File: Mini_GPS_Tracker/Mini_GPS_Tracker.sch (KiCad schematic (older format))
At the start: 23 parts, among them J1 USB_C_Receptacle, J4 Conn_ARM_JTAG_SWD_10, SW1 SW_Push, U1 CH340E, Y1 Crystal

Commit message: updates to routing and fix commit
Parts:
- removed U1: CH340E, Sparkfun-Artemis:MSOP10, symbol Sparkfun~Artemis:CH340E
- added C20: 100 nf, Capacitor_SMD:C_0805_2012Metric, symbol Device:C
- added U1: FT230XS, Package_SO:SSOP-16_3.9x4.9mm_P0.635mm, symbol Interface_USB:FT230XS
- C6, C7: value CAP -> 15 pf
- J4: footprint Connector_PinHeader_1.00mm:PinHeader_2x05_P1.00mm_Vertical -> Connector_PinHeader_2.54mm:PinHeader_2x05_P2.54mm_Vertical
- LS1: symbol Sparkfun~Artemis:CSS-J4D20-SMT -> Mini_GPS_Tracker-rescue:CSS-J4D20-SMT-Sparkfun_Artemis-Mini_GPS_Tracker-rescue
- MD1: symbol Sparkfun~Artemis:SPARKFUN_WRL-15376 -> Mini_GPS_Tracker-rescue:SPARKFUN_WRL-15376-Sparkfun_Artemis-Mini_GPS_Tracker-rescue
- R7: value R -> 0 ohm
- Y1: value Crystal -> 32.786 KHz
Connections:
- wire segments 117 -> 128
- no-connect marks 46 -> 48
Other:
- moved on the sheet: D1, D2, R4, R5, R7

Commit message: Add files via upload
Updates schematics
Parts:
- removed C20: 100 nf, Capacitor_SMD:C_0805_2012Metric, symbol Device:C
- removed C3: 0.1uF, Capacitor_SMD:C_0805_2012Metric_Pad1.15x1.40mm_HandSolder, symbol pspice:CAP
- removed C5: 10nF, Capacitor_SMD:C_0805_2012Metric_Pad1.15x1.40mm_HandSolder, symbol pspice:CAP
- removed C6, C7: 15 pf, Capacitor_SMD:C_0805_2012Metric_Pad1.15x1.40mm_HandSolder, symbol pspice:CAP
- removed D1, D2: LED, LED_SMD:LED_0805_2012Metric_Pad1.15x1.40mm_HandSolder, symbol Device:LED
- removed MD1: SPARKFUN_WRL-15376, Sparkfun-Artemis:SPARKFUN_WRL-15376, symbol Mini_GPS_Tracker-rescue:SPARKFUN_WRL-15376-Sparkfun_Artemis-Mini_GPS_Tracker-re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
- removed R4, R5: 1K, Resistor_SMD:R_0805_2012Metric_Pad1.15x1.40mm_HandSolder, symbol Device:R
- removed U1: FT230XS, Package_SO:SSOP-16_3.9x4.9mm_P0.635mm, symbol Interface_USB:FT230XS
- removed Y1: 32.786 KHz, Crystal:Crystal_SMD_2012-2Pin_2.0x1.2mm_HandSoldering, symbol Device:Crystal
- added C22: 100nF, symbol pspice:CAP
- added J5: Qwiic_Connector, SPARKX_1X04_1MM_RA, symbol SparkFun_SchematicComponents:Qwiic_Connector
- added U12: FT230XS, Package_SO:SSOP-16_3.9x4.9mm_P0.635mm, symbol Interface_USB:FT230XS
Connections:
- net +3V3: now also J5.2 (VCC), U12.12 (VCC)
- net GND: now also C22.1, J5.1 (GND), U12.13 (GND), U12.5 (GND)
- net RTS: now also U12.2 (~RTS)
- net at J1.A7 (D-): now also U12.9 (USBDM)
- net at J1.B7 (D-): now also U12.8 (USBDP)
- new net: C22.2, U12.10 (3V3OUT), U12.11 (~RESET), U12.3 (VCCIO)
- new net QWIIC_SCL: J5.4 (SCL)
- new net QWIIC_SDA: J5.3 (SDA)
- new net USB_RXI: U12.4 (RXD)
- new net USB_TX0: U12.1 (TXD)
- no-connect marks 48 -> 15
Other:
- moved on the sheet: LS1, R7

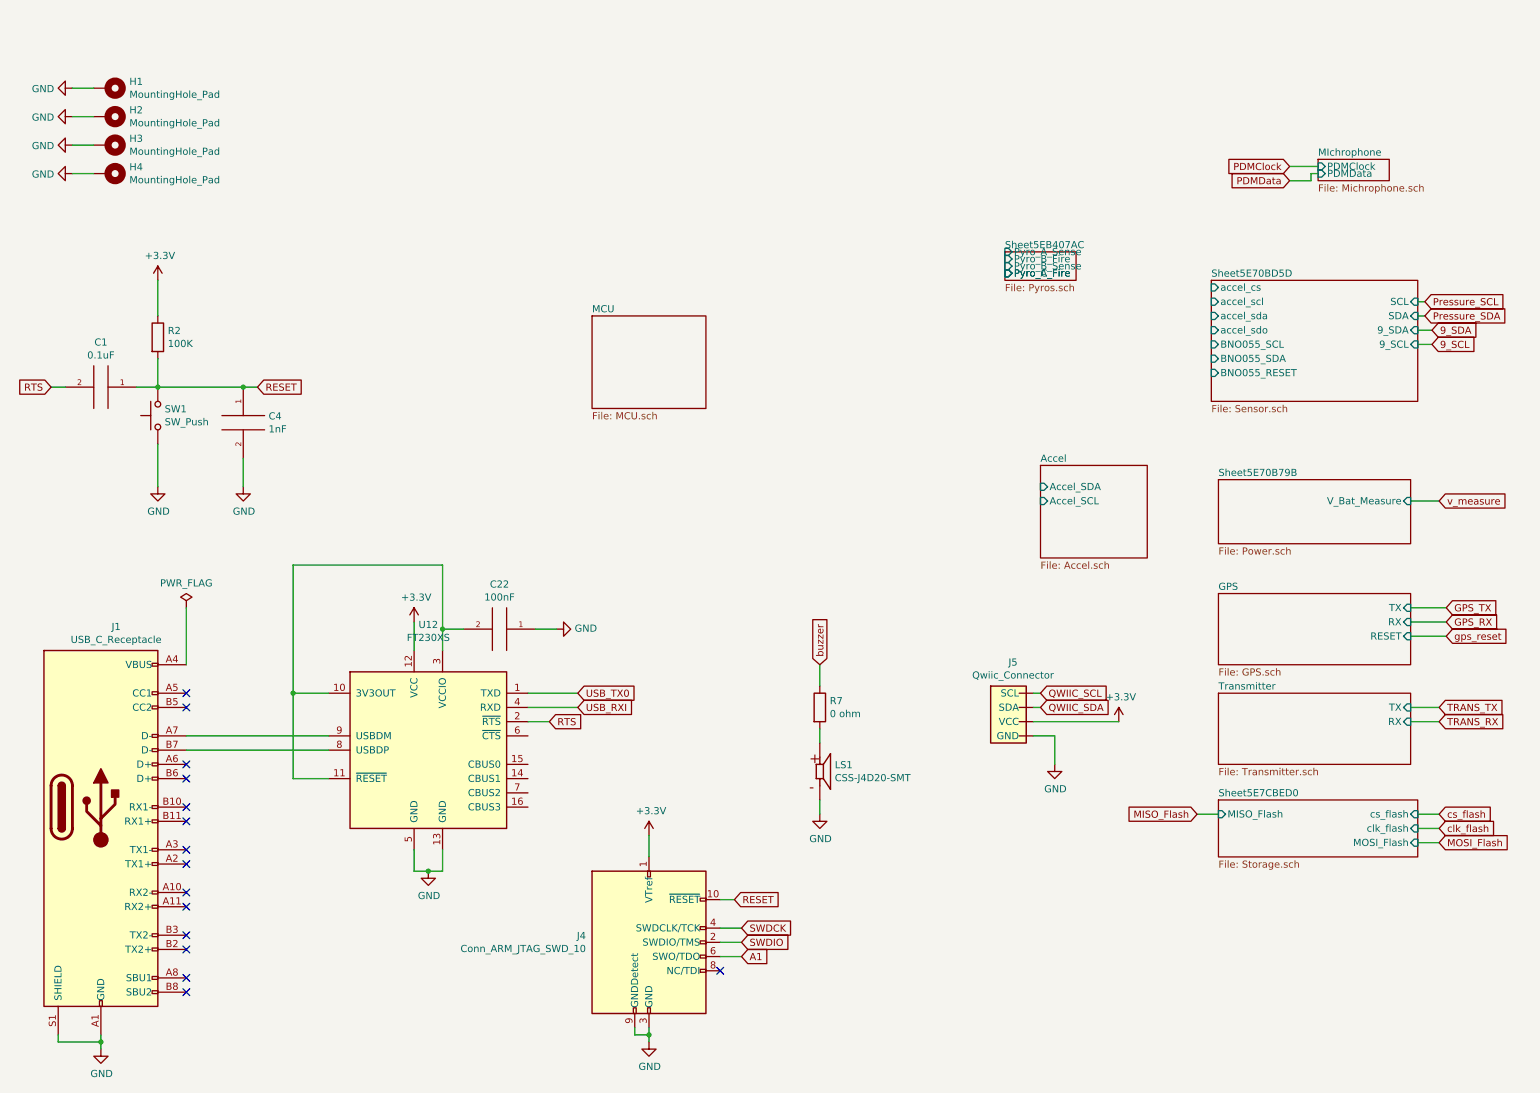
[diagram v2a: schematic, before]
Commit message: Add files via upload
Adding 100 pin MCU
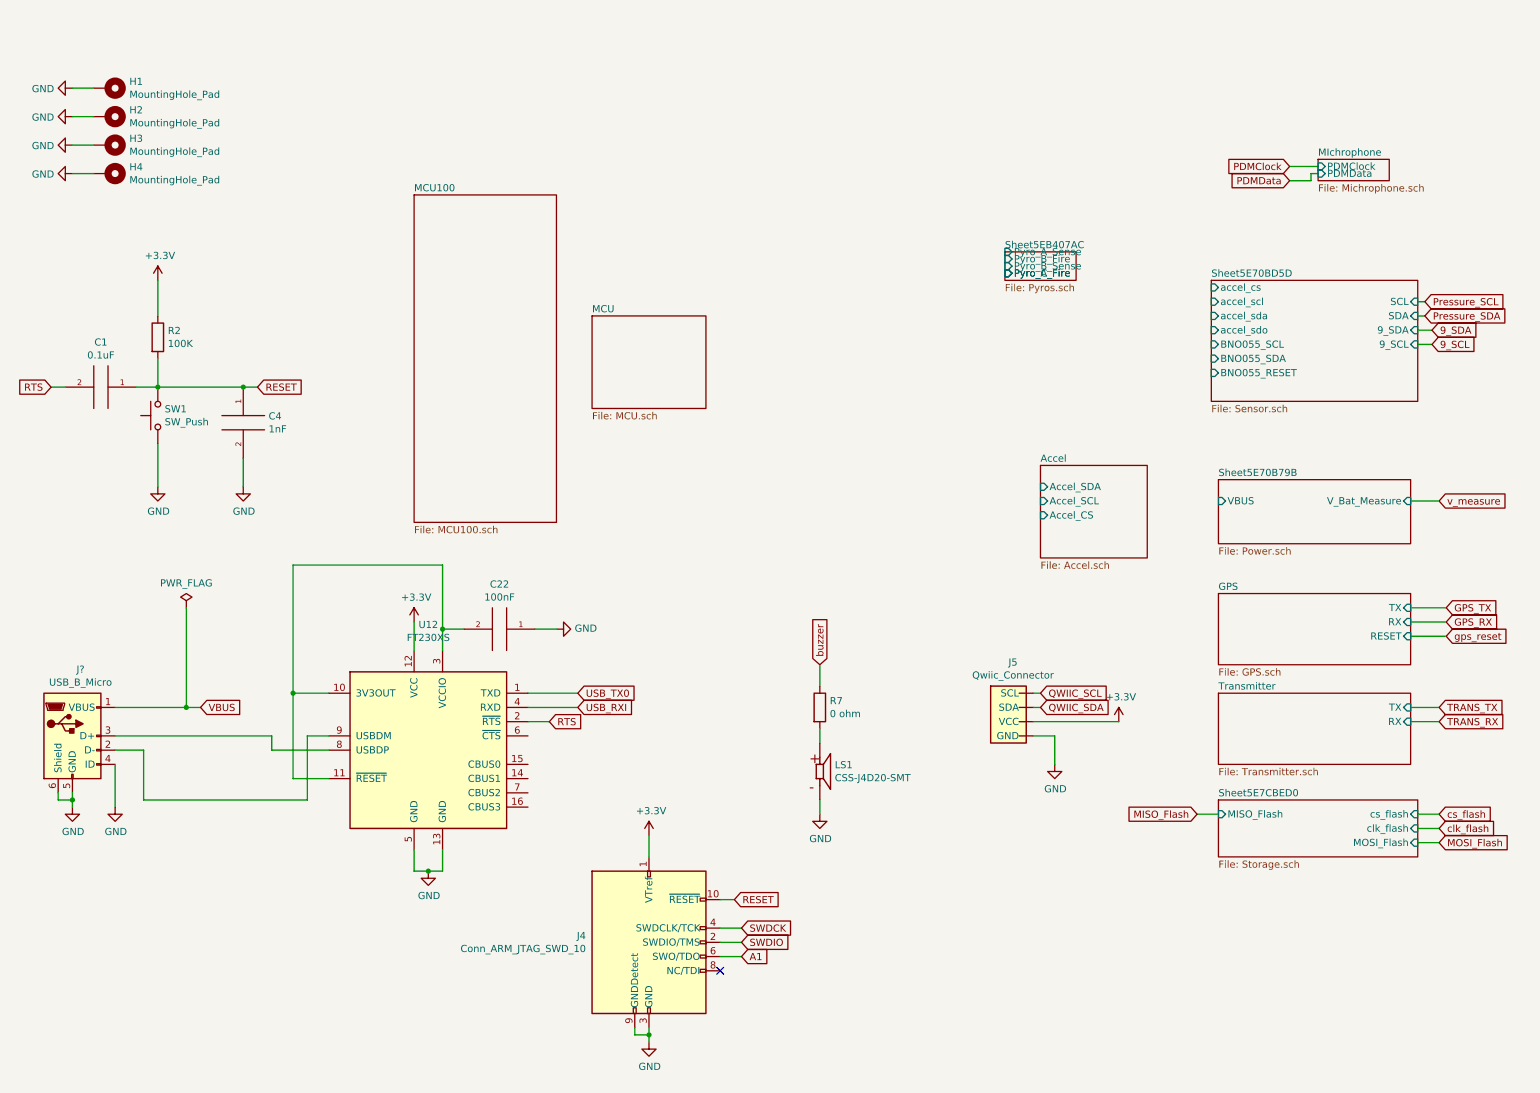
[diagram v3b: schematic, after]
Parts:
- removed J1: USB_C_Receptacle, Connector_USB:USB_C_Receptacle_Amphenol_12401548E4-2A, symbol Connector:USB_C_Receptacle
- added J?: USB_B_Micro, symbol Connector:USB_B_Micro
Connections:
- net GND: now also J?.4 (ID), J?.5 (GND), J?.6 (Shield)
- net at U12.9 (USBDM): now also J?.2 (D-)
- net at U12.8 (USBDP): now also J?.3 (D+)
- new net VBUS: J?.1 (VBUS)
- no-connect marks 15 -> 1
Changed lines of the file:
@@
 EESchema Schematic File Version 4
-LIBS:Mini_GPS_Tracker-cache
 EELAYER 30 0
 EELAYER END
 $Descr A4 11693 8268
 encoding utf-8
-Sheet 1 10
+Sheet 1 11
 Title ""
 Date ""
@@
 L power:GND #PWR02
 U 1 1 5E7614F5
-P 1200 7350
-F 0 "#PWR02" H 1200 7100 50  0001 C CNN
-F 1 "GND" H 1205 7177 50  0000 C CNN
-F 2 "" H 1200 7350 50  0001 C CNN
-F 3 "" H 1200 7350 50  0001 C CNN
-	1    1200 7350
-	1    0    0    -1
-$EndComp
-Wire Wire Line
-	1200 7350 1200 7300
+P 1000 5650
+F 0 "#PWR02" H 1000 5400 50  0001 C CNN
+F 1 "GND" H 1005 5477 50  0000 C CNN
+F 2 "" H 1000 5650 50  0001 C CNN
+F 3 "" H 1000 5650 50  0001 C CNN
+	1    1000 5650
+	1    0    0    -1
+$EndComp
+Wire Wire Line
+	1000 5650 1000 5600
 $Comp
 L power:+3.3V #PWR03
@@
 F1 "Power.sch" 50
 F2 "V_Bat_Measure" I R 10400 3500 50
+F3 "VBUS" I L 9050 3500 50
 $EndSheet
 $Sheet
@@
 Wire Wire Line
 	10400 4450 10650 4450
-Wire Wire Line
-	900  7250 900  7300
-Wire Wire Line
-	900  7300 1200 7300
-Connection ~ 1200 7300
-Wire Wire Line
-	1200 7300 1200 7250
-NoConn ~ 1800 4850
-NoConn ~ 1800 4950
-NoConn ~ 1800 5350
-NoConn ~ 1800 5450
-NoConn ~ 1800 5650
-NoConn ~ 1800 5750
-NoConn ~ 1800 5950
-NoConn ~ 1800 6050
-NoConn ~ 1800 6250
-NoConn ~ 1800 6350
-NoConn ~ 1800 6550
-NoConn ~ 1800 6650
-NoConn ~ 1800 6850
-NoConn ~ 1800 6950
+Connection ~ 1000 5600
+Wire Wire Line
+	1000 5600 1000 5550
 Text GLabel 10550 2300 2    50   Input ~ 0
 9_SDA
@@
 	6250 4650 6250 4800
 $Comp
-L Connector:USB_C_Receptacle J1
-U 1 1 5E74492E
-P 1200 5650
-F 0 "J1" H 1307 6917 50  0000 C CNN
-F 1 "USB_C_Receptacle" H 1307 6826 50  0000 C CNN
-F 2 "Connector_USB:USB_C_Receptacle_Amphenol_12401548E4-2A" H 1350 5650 50  0001 C CNN
-F 3 "https://www.usb.org/sites/default/files/documents/usb_type-c.zip" H 1350 5650 50  0001 C CNN
-	1    1200 5650
-	1    0    0    -1
-$EndComp
-$Comp
 L power:PWR_FLAG #FLG0104
 U 1 1 5E8392C8
@@
 	1    0    0    -1
 $EndComp
-Wire Wire Line
-	1800 4250 1800 4650
 $Comp
 L power:+3.3V #PWR030
@@
 	1    0    0    -1
 $EndComp
-Wire Wire Line
-	1800 5150 2800 5150
-Wire Wire Line
-	1800 5250 2800 5250
 $Comp
 L power:GND #PWR0130
@@
 F2 "Accel_SDA" I L 7800 3400 50
 F3 "Accel_SCL" I L 7800 3500 50
+F4 "Accel_CS" I L 7800 3600 50
+$EndSheet
+Wire Wire Line
+	900  5550 900  5600
+Wire Wire Line
+	900  5600 1000 5600
+Text GLabel 1900 4950 2    50   Input ~ 0
+VBUS
+Wire Wire Line
+	1800 4250 1800 4950
+Connection ~ 1800 4950
+Wire Wire Line
+	1800 4950 1900 4950
+Wire Wire Line
+	1300 4950 1800 4950
+$Comp
+L Connector:USB_B_Micro J?
+U 1 1 5EA00C58
+P 1000 5150
+F 0 "J?" H 1057 5617 50  0000 C CNN
+F 1 "USB_B_Micro" H 1057 5526 50  0000 C CNN
+F 2 "" H 1150 5100 50  0001 C CNN
+F 3 "~" H 1150 5100 50  0001 C CNN
+	1    1000 5150
+	1    0    0    -1
+$EndComp
+$Comp
+L power:GND #PWR?
+U 1 1 5EA017A3
+P 1300 5650
+F 0 "#PWR?" H 1300 5400 50  0001 C CNN
+F 1 "GND" H 1305 5477 50  0000 C CNN
+F 2 "" H 1300 5650 50  0001 C CNN
+F 3 "" H 1300 5650 50  0001 C CNN
+	1    1300 5650
+	1    0    0    -1
+$EndComp
+Wire Wire Line
+	1300 5350 1300 5650
+Wire Wire Line
+	1300 5150 2400 5150
+Wire Wire Line
+	2400 5150 2400 5250
+Wire Wire Line
+	2400 5250 2800 5250
+Wire Wire Line
+	2800 5150 2650 5150
+Wire Wire Line
+	2650 5150 2650 5600
+Wire Wire Line
+	2650 5600 1500 5600
+Wire Wire Line
+	1500 5600 1500 5250
+Wire Wire Line
+	1500 5250 1300 5250
+$Sheet
+S 3400 1350 1000 2300
+U 5EA0B5A0
+F0 "MCU100" 50
+F1 "MCU100.sch" 50
 $EndSheet
 $EndSCHEMATC

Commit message: Add files via upload
Making update for 100 pin CPU
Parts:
- gave numbers to parts that had none: 1
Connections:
- net A1 renamed SWO
- net USB_RXI renamed USB_RX
- net USB_TX0 renamed USB_TX
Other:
- moved on the sheet: LS1, R7
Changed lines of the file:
@@
 EESchema Schematic File Version 4
+LIBS:Mini_GPS_Tracker-cache
 EELAYER 30 0
 EELAYER END
 $Descr A4 11693 8268
 encoding utf-8
-Sheet 1 11
+Sheet 1 7
 Title ""
 Date ""
@@
 F11 "BNO055_SDA" I L 9000 2500 50
 F12 "BNO055_RESET" I L 9000 2600 50
+F13 "BNO055_INTERRUPT" I L 9000 2700 50
 $EndSheet
 Wire Wire Line
@@
 F2 "TX" I R 10400 4950 50
 F3 "RX" I R 10400 5050 50
+F4 "murata_tx" I L 9050 4900 50
+F5 "murata_rx" I L 9050 5000 50
+F6 "murata_rts" I L 9050 5100 50
+F7 "murata_cts" I L 9050 5200 50
 $EndSheet
 Text GLabel 10600 3500 2    50   Input ~ 0
@@
 L Mini_GPS_Tracker-rescue:CSS-J4D20-SMT-Sparkfun_Artemis-Mini_GPS_Tracker-rescue LS1
 U 1 1 5E7E01A2
-P 6250 5400
-F 0 "LS1" H 6355 5446 50  0000 L CNN
-F 1 "CSS-J4D20-SMT" H 6355 5355 50  0000 L CNN
-F 2 "Sparkfun-Artemis:CUI_CSS-J4D20-SMT" H 6250 5400 50  0001 L BNN
-F 3 "CUI" H 6250 5400 50  0001 L BNN
-F 4 "None" H 6250 5400 50  0001 L BNN "Field4"
-F 5 "CSS-J4D20-SMT" H 6250 5400 50  0001 L BNN "Field5"
-F 6 "Unavailable" H 6250 5400 50  0001 L BNN "Field6"
-F 7 "8.5 mm, 3.6 V, 90 dB, Surface Mount _SMT_, Magnetic Audio Transducer Buzzer" H 6250 5400 50  0001 L BNN "Field7"
-F 8 "None" H 6250 5400 50  0001 L BNN "Field8"
-	1    6250 5400
+P 6500 6250
+F 0 "LS1" H 6605 6296 50  0000 L CNN
+F 1 "CSS-J4D20-SMT" H 6605 6205 50  0000 L CNN
+F 2 "Sparkfun-Artemis:CUI_CSS-J4D20-SMT" H 6500 6250 50  0001 L BNN
+F 3 "CUI" H 6500 6250 50  0001 L BNN
+F 4 "None" H 6500 6250 50  0001 L BNN "Field4"
+F 5 "CSS-J4D20-SMT" H 6500 6250 50  0001 L BNN "Field5"
+F 6 "Unavailable" H 6500 6250 50  0001 L BNN "Field6"
+F 7 "8.5 mm, 3.6 V, 90 dB, Surface Mount _SMT_, Magnetic Audio Transducer Buzzer" H 6500 6250 50  0001 L BNN "Field7"
+F 8 "None" H 6500 6250 50  0001 L BNN "Field8"
+	1    6500 6250
 	1    0    0    -1
 $EndComp
@@
 L Device:R R7
 U 1 1 5E7E2738
-P 6250 4950
-F 0 "R7" H 6320 4996 50  0000 L CNN
-F 1 "0 ohm" H 6320 4905 50  0000 L CNN
-F 2 "Resistor_SMD:R_0805_2012Metric_Pad1.15x1.40mm_HandSolder" V 6180 4950 50  0001 C CNN
-F 3 "~" H 6250 4950 50  0001 C CNN
-	1    6250 4950
+P 6500 5800
+F 0 "R7" H 6570 5846 50  0000 L CNN
+F 1 "0 ohm" H 6570 5755 50  0000 L CNN
+F 2 "Resistor_SMD:R_0805_2012Metric_Pad1.15x1.40mm_HandSolder" V 6430 5800 50  0001 C CNN
+F 3 "~" H 6500 5800 50  0001 C CNN
+	1    6500 5800
 	1    0    0    -1
 $EndComp
@@
 L power:GND #PWR0116
 U 1 1 5E7E36E3
-P 6250 5700
-F 0 "#PWR0116" H 6250 5450 50  0001 C CNN
-F 1 "GND" H 6255 5527 50  0000 C CNN
-F 2 "" H 6250 5700 50  0001 C CNN
-F 3 "" H 6250 5700 50  0001 C CNN
-	1    6250 5700
-	1    0    0    -1
-$EndComp
-Wire Wire Line
-	6250 5600 6250 5700
-Wire Wire Line
-	6250 5200 6250 5100
-Text GLabel 6250 4650 1    50   Input ~ 0
+P 6500 6550
+F 0 "#PWR0116" H 6500 6300 50  0001 C CNN
+F 1 "GND" H 6505 6377 50  0000 C CNN
+F 2 "" H 6500 6550 50  0001 C CNN
+F 3 "" H 6500 6550 50  0001 C CNN
+	1    6500 6550
+	1    0    0    -1
+$EndComp
+Wire Wire Line
+	6500 6450 6500 6550
+Wire Wire Line
+	6500 6050 6500 5950
+Text GLabel 6500 5500 1    50   Input ~ 0
 buzzer
 Wire Wire Line
-	6250 4650 6250 4800
+	6500 5500 6500 5650
 $Comp
 L power:PWR_FLAG #FLG0104
@@
 RESET
 Text GLabel 5700 6700 2    50   Input ~ 0
-A1
+SWO
 Wire Wire Line
 	5050 7250 5050 7300
@@
 	4200 5050 4350 5050
 Text GLabel 4550 4950 2    50   Input ~ 0
-USB_RXI
+USB_RX
 Text GLabel 4550 4850 2    50   Input ~ 0
-USB_TX0
+USB_TX
 Wire Wire Line
 	4200 4850 4550 4850
@@
 Wire Wire Line
 	2550 4850 2550 3950
-$Sheet
-S 9750 1100 500  150
-U 5EA9D17A
-F0 "MIchrophone" 50
-F1 "Michrophone.sch" 50
-F2 "PDMClock" I L 9750 1150 50
-F3 "PDMData" I L 9750 1200 50
-$EndSheet
-Text GLabel 9550 1150 0    50   Input ~ 0
-PDMClock
-Text GLabel 9550 1250 0    50   Input ~ 0
-PDMData
-Wire Wire Line
-	9550 1150 9750 1150
-Wire Wire Line
-	9550 1250 9700 1250
-Wire Wire Line
-	9700 1250 9700 1200
-Wire Wire Line
-	9700 1200 9750 1200
 $Comp
 L SparkFun_SchematicComponents:Qwiic_Connector J5
@@
 Wire Wire Line
 	7750 4950 7800 4950
-$Sheet
-S 7550 1750 500  200
-U 5EB407AD
-F0 "Sheet5EB407AC" 50
-F1 "Pyros.sch" 50
-F2 "Pyro_A_Fire" I L 7550 1900 50
-F3 "Pyro_A_Sense" I L 7550 1750 50
-F4 "Pyro_B_Fire" I L 7550 1800 50
-F5 "Pyro_B_Sense" I L 7550 1850 50
-F6 "Pyro_C_Fire" I L 7550 1900 50
-$EndSheet
-$Sheet
-S 4650 2200 800  650
-U 5E9FE63A
-F0 "MCU" 50
-F1 "MCU.sch" 50
-$EndSheet
-$Sheet
-S 7800 3250 750  650
-U 5E9E34E6
-F0 "Accel" 50
-F1 "Accel.sch" 50
-F2 "Accel_SDA" I L 7800 3400 50
-F3 "Accel_SCL" I L 7800 3500 50
-F4 "Accel_CS" I L 7800 3600 50
-$EndSheet
 Wire Wire Line
 	900  5550 900  5600
@@
 	1300 4950 1800 4950
 $Comp
-L Connector:USB_B_Micro J?
+L Connector:USB_B_Micro J1
 U 1 1 5EA00C58
 P 1000 5150
-F 0 "J?" H 1057 5617 50  0000 C CNN
+F 0 "J1" H 1057 5617 50  0000 C CNN
 F 1 "USB_B_Micro" H 1057 5526 50  0000 C CNN
 F 2 "" H 1150 5100 50  0001 C CNN
@@
 $EndComp
 $Comp
-L power:GND #PWR?
+L power:GND #PWR01
 U 1 1 5EA017A3
 P 1300 5650
-F 0 "#PWR?" H 1300 5400 50  0001 C CNN
+F 0 "#PWR01" H 1300 5400 50  0001 C CNN
 F 1 "GND" H 1305 5477 50  0000 C CNN
 F 2 "" H 1300 5650 50  0001 C CNN
@@
 	1500 5250 1300 5250
 $Sheet
-S 3400 1350 1000 2300
+S 3100 700  4400 2950
 U 5EA0B5A0
 F0 "MCU100" 50
 F1 "MCU100.sch" 50
+F2 "RESET" I L 3100 950 50
+F3 "Pressure_SDA" I L 3100 1050 50
+F4 "Pressure_SCL" I L 3100 1150 50
+F5 "GPS_TX" I L 3100 1250 50
+F6 "GPS_RX" I L 3100 1350 50
+F7 "Accel_CS" I L 3100 3350 50
+F8 "Accel_SCL" I L 3100 3450 50
+F9 "Accel_SDA" I L 3100 3550 50
+F10 "buzzer" I L 3100 1950 50
+F11 "SW0" I L 3100 2050 50
+F12 "cs_flash" I L 3100 2700 50
+F13 "gps_reset" I L 3100 1450 50
+F14 "SWDCK" I L 3100 2150 50
+F15 "SWDIO" I L 3100 2250 50
+F16 "MOSI_Flash" I L 3100 2500 50
+F17 "MISO_Flash" I L 3100 2600 50
+F18 "USB_RX" I L 3100 2800 50
+F19 "clk_flash" I L 3100 2400 50
+F20 "v_measure" I L 3100 3100 50
+F21 "TRANS_TX" I R 7500 1050 50
+F22 "TRANS_RX" I R 7500 1150 50
+F23 "QWIIC_SCL" I R 7500 1800 50
+F24 "QWIIC_SDA" I R 7500 1900 50
+F25 "USB_TX" I L 3100 2900 50
+F26 "BNO055_SCL" I R 7500 2300 50
+F27 "BNO055_SDA" I R 7500 2400 50
+F28 "BNO055_Interrupt" I R 7500 2550 50
+F29 "BNO055_Reset" I R 7500 2700 50
+F30 "murata_tx" I R 7500 3000 50
+F31 "murata_rx" I R 7500 3100 50
+F32 "murata_cts" I R 7500 3200 50
+F33 "murata_rts" I R 7500 3300 50
 $EndSheet
 $EndSCHEMATC

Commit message: Add files via upload
Splitting board into modules
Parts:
- removed C1: 0.1uF, Capacitor_SMD:C_0805_2012Metric_Pad1.15x1.40mm_HandSolder, symbol pspice:CAP
- removed C22: 100nF, symbol pspice:CAP
- removed C4: 1nF, Capacitor_SMD:C_0805_2012Metric_Pad1.15x1.40mm_HandSolder, symbol pspice:CAP
- removed H1, H2, H3, H4: MountingHole_Pad, MountingHole:MountingHole_3.2mm_M3, symbol Mechanical:MountingHole_Pad
- removed J1: USB_B_Micro, symbol Connector:USB_B_Micro
- removed J4: Conn_ARM_JTAG_SWD_10, Connector_PinHeader_2.54mm:PinHeader_2x05_P2.54mm_Vertical, symbol Connector:Conn_ARM_JTAG_SWD_10
- removed J5: Qwiic_Connector, SPARKX_1X04_1MM_RA, symbol SparkFun_SchematicComponents:Qwiic_Connector
- removed LS1: CSS-J4D20-SMT, Sparkfun-Artemis:CUI_CSS-J4D20-SMT, symbol Mini_GPS_Tracker-rescue:CSS-J4D20-SMT-Sparkfun_Artemis-Mini_GPS_Tracker-rescue
- removed R2: 100K, Resistor_SMD:R_0805_2012Metric_Pad1.15x1.40mm_HandSolder, symbol Device:R
- removed R7: 0 ohm, Resistor_SMD:R_0805_2012Metric_Pad1.15x1.40mm_HandSolder, symbol Device:R
- removed SW1: SW_Push, Sparkfun-Artemis:SW_TL1015AF160QG, symbol Switch:SW_Push
- removed U12: FT230XS, Package_SO:SSOP-16_3.9x4.9mm_P0.635mm, symbol Interface_USB:FT230XS
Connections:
- no-connect marks 1 -> 0
